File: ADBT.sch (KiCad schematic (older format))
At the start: 108 parts, among them J1 ADB1, J2 microUSB, J3 JTAG, Q1 AO3401, Q2 MMBT3904, Q3 MMBT3904, Q4 MMBT3904, Q5 MMBT3904, Q6 AO3401, SW1 SW_Push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

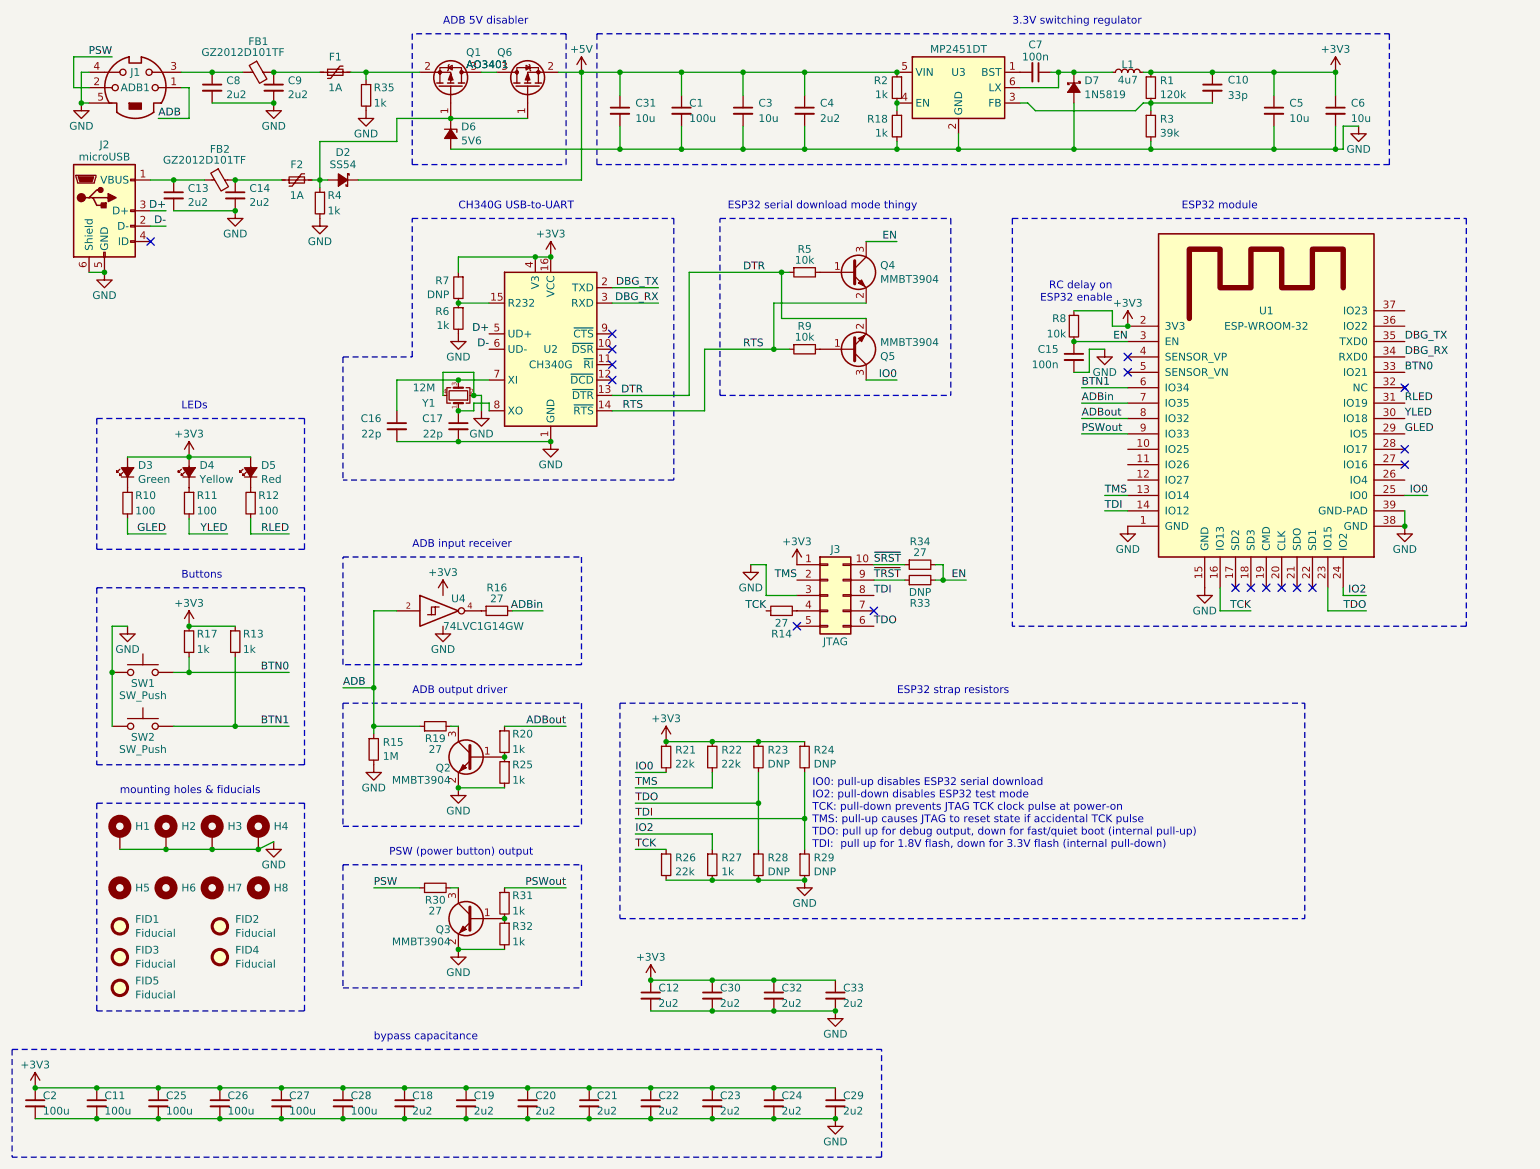
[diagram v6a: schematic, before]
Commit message: Change caps to fix power issue
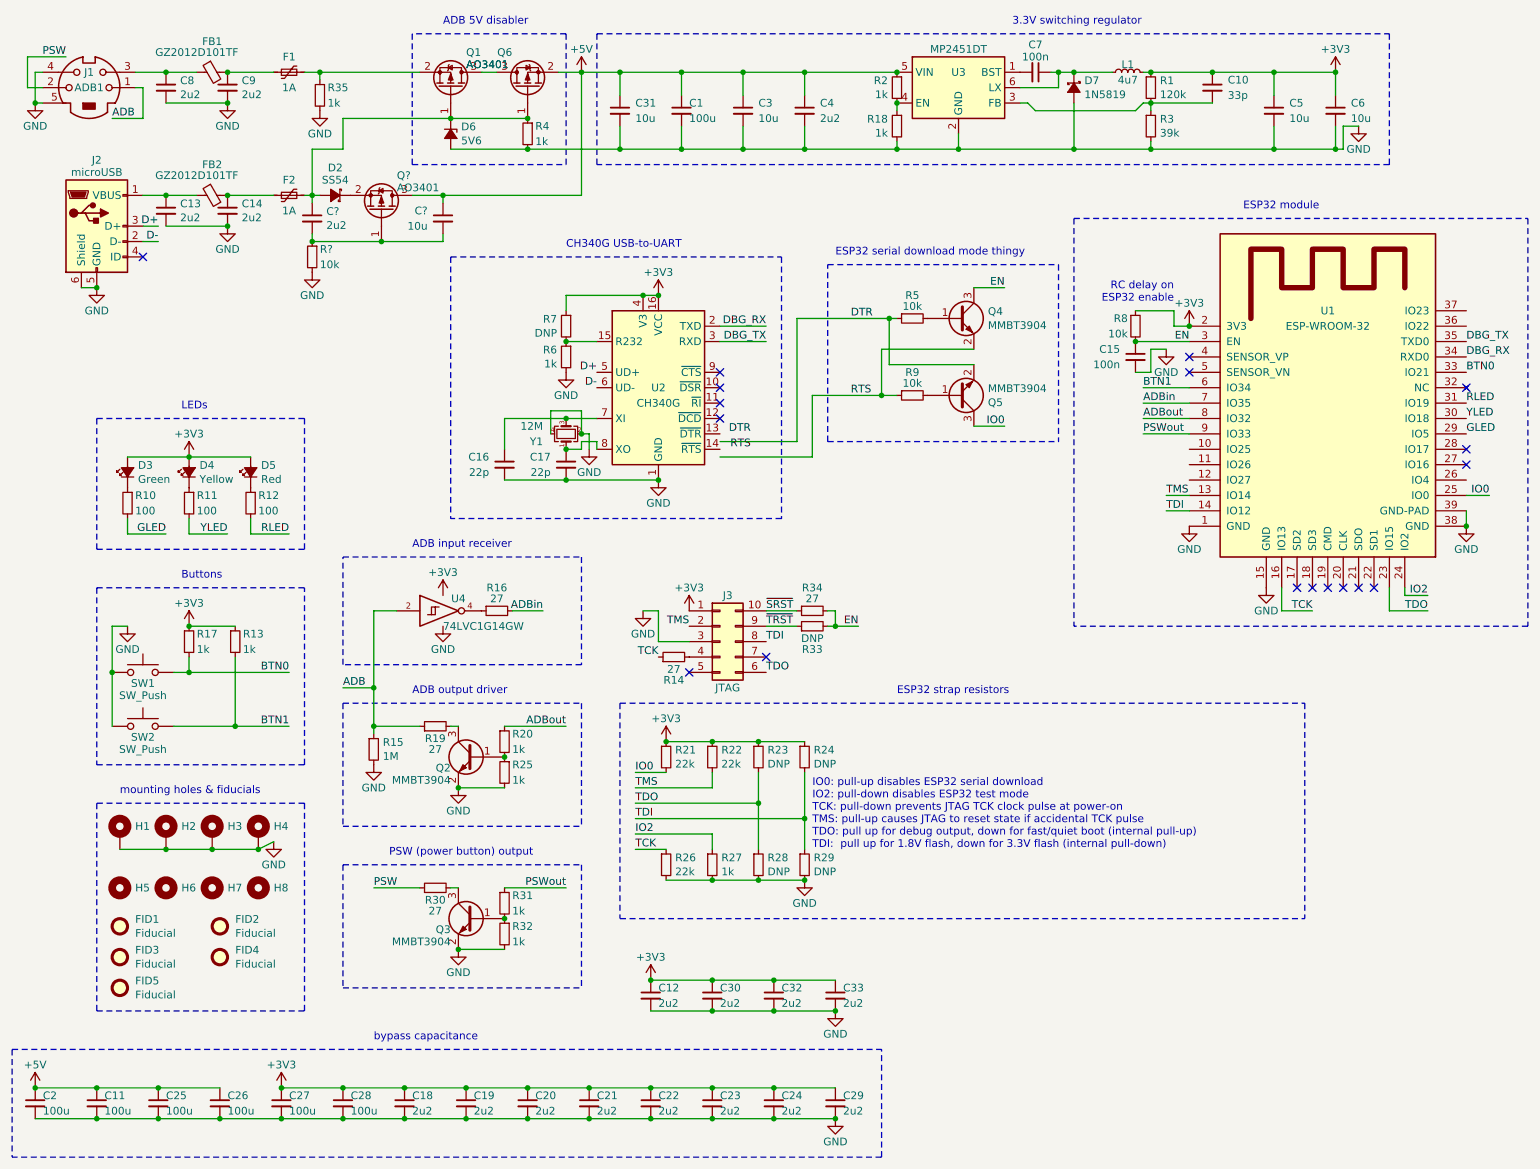
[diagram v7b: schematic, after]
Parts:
- added C?: 2u2, stdpads:C_0603, symbol Device:C_Small
- added C?: 10u, stdpads:C_0805, symbol Device:C_Small
- added Q?: AO3401, stdpads:SOT-23, symbol Device:Q_PMOS_GSD
- added R?: 10k, stdpads:R_0603, symbol Device:R_Small
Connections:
- net +3V3: no longer C11.1, C2.1, C25.1, C26.1
- net +5V: now also C11.1, C2.1, C25.1, C26.1, C?.1, Q?.3 (D); no longer D2.1 (K)
- net DBG_RX: now also U2.2 (TXD); no longer U2.3 (RXD)
- net DBG_TX: now also U2.3 (RXD); no longer U2.2 (TXD)
- net DTR: no longer U2.13 (~DTR)
- net GND: now also R?.2
- net RTS: no longer U2.14 (~RTS)
- net at D2.2 (A), D6.1 (K), F2.2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: now also C?.1
- new net: C?.2, C?.2, Q?.1 (G), R?.1
- new net: D2.1 (K), Q?.2 (S)
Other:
- moved on the sheet: C13, C14, C15, C16, C17, C8, C9, D2, F1, F2, FB1, FB2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
